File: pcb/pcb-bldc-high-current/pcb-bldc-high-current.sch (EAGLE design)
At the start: 87 parts, among them Q1 MOSFET_NHL60N04D, Q2 MOSFET_NHL60N04D, Q3 MOSFET_NHL60N04D, Q4 MOSFET_NHL60N04D, Q5 MOSFET_NHL60N04D, Q6 MOSFET_NHL60N04D, U1 AS5600, U2 LCT485_BUS_TRANSCEIVER, U3 LCT485_BUS_TRANSCEIVER, U4 HX712_CURR_SENS, U5 STM32G070RBT6, U6 LDO-HT71XX, U7 LDO-HT71XX, X1 PIN_3X2HD, X2 PIN_1X1WELDINGTERMINAL, X3 PIN_1X1WELDINGTERMINAL, X4 PIN_1X1WIRE1, X5 PIN_5X1HD, X6 PIN_1X1WIRE1, X7 PIN_1X1WIRE1, X9 06-JST-B6B-XH-A, Y1 3213-QUARZ3225

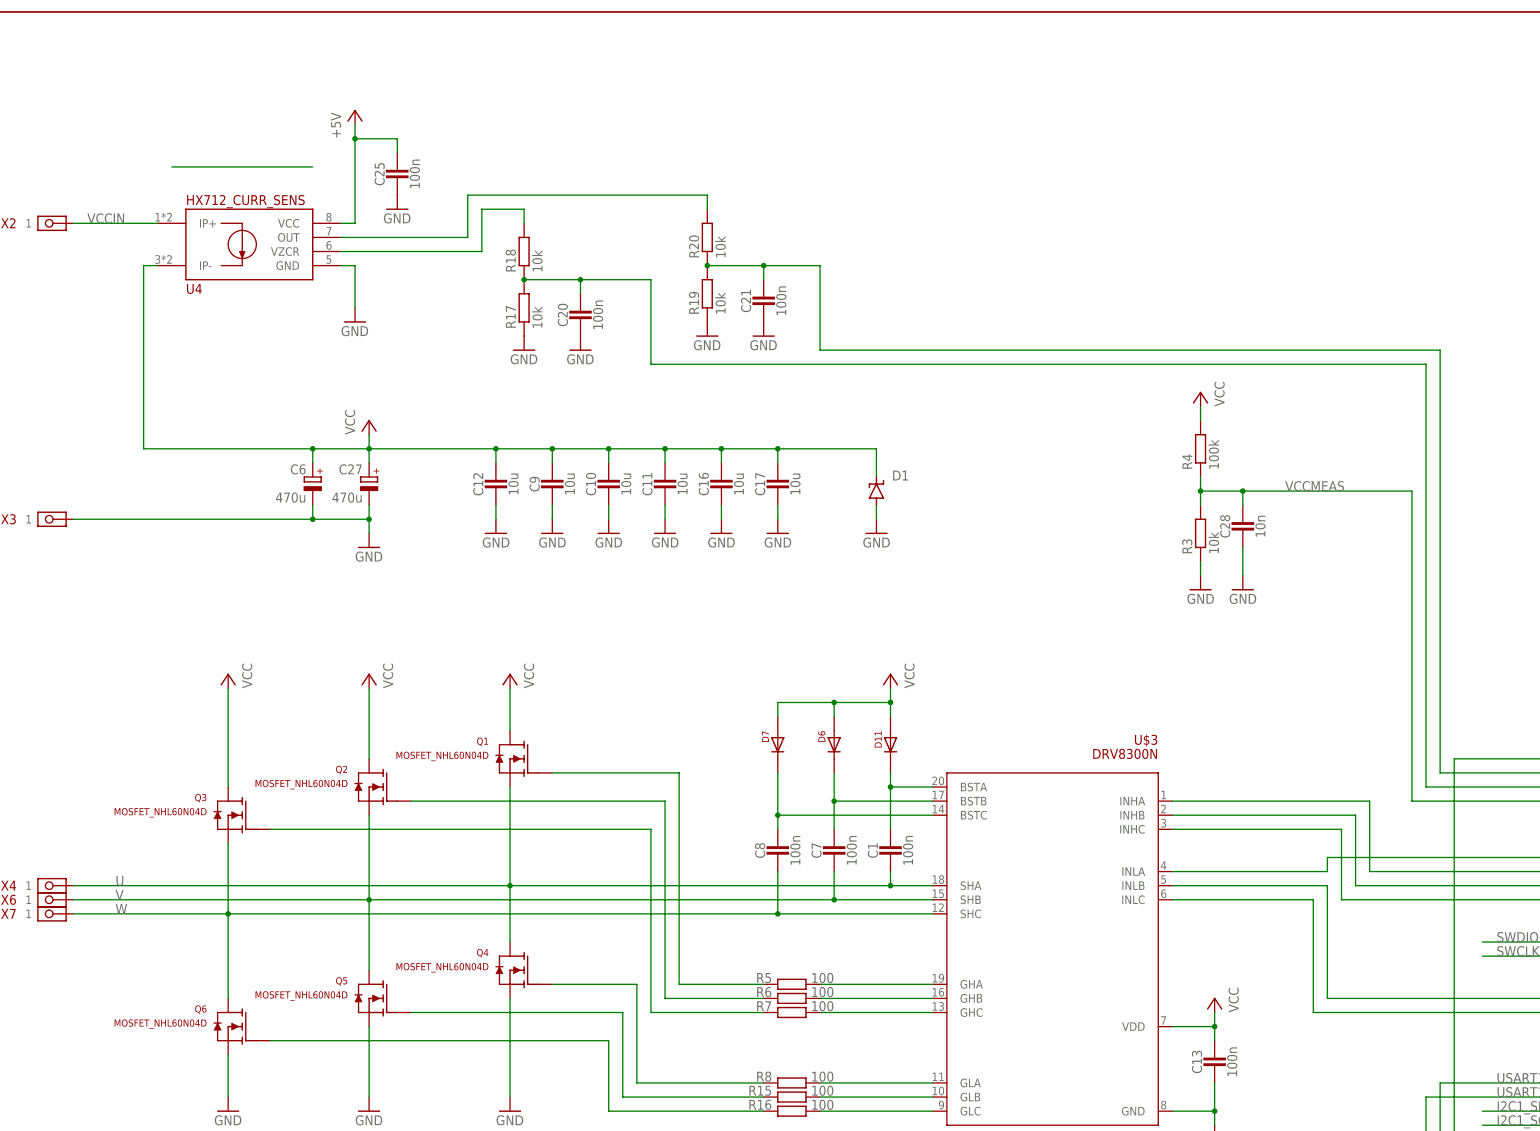
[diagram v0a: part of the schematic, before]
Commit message: 2 rs485 drivers
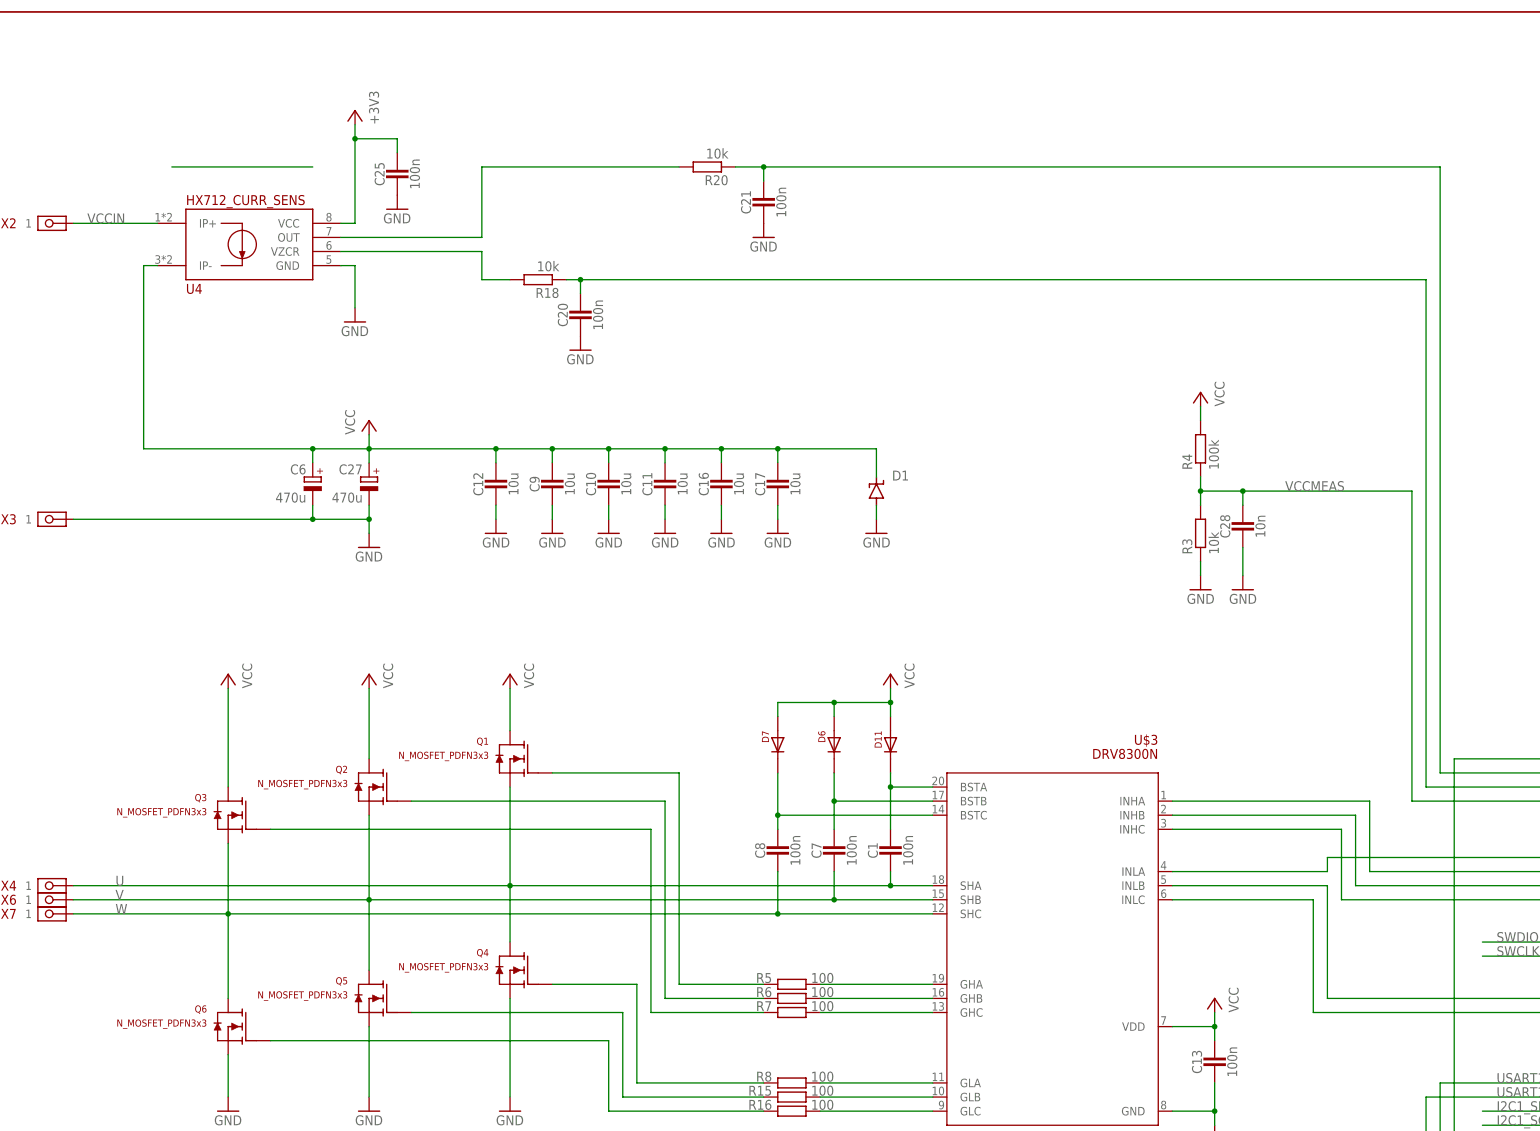
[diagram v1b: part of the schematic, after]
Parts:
- removed R17, R19: 10k, passives:RESISTOR0603_RES
- Q1, Q2, Q3, Q4, Q5, Q6: value MOSFET_NHL60N04D -> N_MOSFET_PDFN3x3
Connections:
- net +3V3: now also C25.1, U4.VCC
- net +5V: no longer C25.1, U4.VCC
- net GND: no longer R17.1, R19.1
- net N$41: no longer R17.2
- net N$42: no longer R19.2
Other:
- moved on the sheet: C21, R18, R20

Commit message: pcb release high current
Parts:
- removed C30: 100n, passives:CAPACITOR0603_CAP
- removed X9: 06-JST-B6B-XH-A, bt_con-jst-xh:06-JST-B6B-XH-A
- added C31, C32: 100n, passives:CAPACITOR0603_CAP
- added J2: GT-USB-7010, ftobler:GT-USB-7010
- added R17, R19: 5k1, passives:RESISTOR0603_RES
- added R21, R22: 4k7, passives:RESISTOR0603_RES
- added R23, R24: 100, passives:RESISTOR0603_RES
- added U$4: 03-JST-B3B-XH-A, bt_con-jst-xh:03-JST-B3B-XH-A
- U$2: value LOGO-TOBENG-4MM-MASK -> LOGO-0.25MM; device ftobler:LOGO-TOBENG-4MM-MASK -> ftobler:LOGO-0.25MM
- U3: value LCT485_BUS_TRANSCEIVER -> CH340X; device ftobler:LCT485_BUS_TRANSCEIVER -> ftobler:CH340X
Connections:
- removed net N$38: U3.B, X9-3.1
- removed net N$39: U3.A, X9-4.1
- new net 485A: U$4-2.1, U2.A
- new net 485B: U$4-1.1, U2.B
- new net DTR: R22.1, U3.DTR#, U5.PC13
- new net N$51: J2.CC2, R17.2
- new net N$52: J2.CC1, R19.2
- new net N$53: C31.1, U3.V3
- new net USB_N: J2.DN1, J2.DN2, U3.UD-
- new net USB_P: J2.DP1, J2.DP2, U3.UD+
- net +3V3: no longer X9-5.1
- net +5V: no longer C30.1, U3.VCC
- net GND: now also C31.2, C32.2, J2.GND1, J2.GND2, J2.SHIELD, R17.1, R19.1, R22.2, U$4-3.1; no longer C30.2, X9-6.1
- net N$1: now also R23.2, U3.TXD; no longer U2.RE, U5.PC13
- net N$36: now also C32.1, J2.VBUS1, J2.VBUS2, U3.VCC; no longer U2.B, X9-1.1
- net N$37: now also R21.2, U3.RTS#; no longer U2.A, X9-2.1
- net N$45: now also U2.RO; no longer U3.RO
- net N$46: now also U2.RE; no longer U3.RE
- net N$47: now also U2.DE; no longer U3.DE
- net N$48: now also U2.DI; no longer U3.DI
- net N$5: now also R24.2, U3.RXD; no longer U2.DE, U5.PC12
- net NRST: now also R21.1
- net USART1_RX: now also R23.1; no longer U2.RO
- net USART1_TX: now also R24.1; no longer U2.DI
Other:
- moved on the sheet: C14, C15, C26, R10, R9, U1, U2
